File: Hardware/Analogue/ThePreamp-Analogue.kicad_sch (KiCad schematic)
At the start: 37 parts, among them IC1 ULN2803CDWR, J1 To preamp, J10 Switch & trigger outputs and 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, J11 Conn_01x04, J12 Conn_01x03, J13 Conn_01x04, J14 Conn_01x03, J15 Conn_01x02_Pin, J2 From preamp, J3 Digital In, J4 Digital Pass Through, J5 Conn_01x03_Pin, J9 ADS1115, K1 Input 1, K2 Input 5 (opt.), K3 Input 2, K4 Input 3, K5 Input 4, K6 Output Mute, K7 Trigger 1, K8 Trigger 2, U1 MCP23008-E_SO

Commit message: Chassis placement new draft
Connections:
- net +12V: now also J3.12 (Pin_12), J3.14 (Pin_14), J3.16 (Pin_16); no longer J3.2 (Pin_2), J3.4 (Pin_4)
- net +3.3V: now also J3.8 (Pin_8)
- net GND: now also J3.2 (Pin_2), J3.4 (Pin_4); no longer J3.12 (Pin_12), J3.14 (Pin_14), J3.16 (Pin_16), J3.8 (Pin_8)
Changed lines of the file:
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@@
 	)
 	(junction
-		(at 128.27 238.252)
-		(diameter 0)
-		(color 0 0 0 0)
-	)
-	(junction
-		(at 125.73 220.472)
-		(diameter 0)
-		(color 0 0 0 0)
-	)
-	(junction
 		(at 327.66 63.5)
 		(diameter 0)
@@
 	)
 	(junction
-		(at 131.318 225.552)
+		(at 128.27 221.742)
 		(diameter 0)
 		(color 0 0 0 0)
 	)
 	(junction
-		(at 128.27 235.712)
+		(at 128.27 228.092)
 		(diameter 0)
 		(color 0 0 0 0)
 	)
 	(junction
-		(at 128.27 233.172)
+		(at 128.27 235.712)
 		(diameter 0)
 		(color 0 0 0 0)
@@
 	(wire
 		(pts
-			(xy 131.318 230.632) (xy 131.318 225.552)
+			(xy 128.27 230.632) (xy 128.27 228.092)
 		)
 		(stroke
@@
 	(wire
 		(pts
-			(xy 335.28 67.31) (xy 354.33 67.31)
+			(xy 128.27 220.472) (xy 125.73 220.472)
 		)
 		(stroke
@@
 	(wire
 		(pts
-			(xy 86.614 200.66) (xy 99.06 200.66)
+			(xy 335.28 67.31) (xy 354.33 67.31)
 		)
 		(stroke
@@
 	(wire
 		(pts
-			(xy 262.382 71.12) (xy 262.382 73.66)
+			(xy 86.614 200.66) (xy 99.06 200.66)
 		)
 		(stroke
@@
 	(wire
 		(pts
-			(xy 131.064 238.252) (xy 128.27 238.252)
+			(xy 262.382 71.12) (xy 262.382 73.66)
 		)
 		(stroke
@@
 	(wire
 		(pts
-			(xy 128.27 228.092) (xy 128.27 233.172)
-		)
-		(stroke
-			(width 0)
-			(type default)
-		)
-	)
-	(wire
-		(pts
 			(xy 125.73 233.172) (xy 128.27 233.172)
 		)
@@
 	(wire
 		(pts
-			(xy 125.73 230.632) (xy 131.318 230.632)
+			(xy 125.73 230.632) (xy 128.27 230.632)
 		)
 		(stroke
@@
 	(wire
 		(pts
-			(xy 125.73 223.012) (xy 125.73 220.472)
+			(xy 128.27 228.092) (xy 128.27 225.552)
+		)
+		(stroke
+			(width 0)
+			(type default)
+		)
+	)
+	(wire
+		(pts
+			(xy 128.27 223.012) (xy 128.27 221.742)
 		)
 		(stroke
@@
 	(wire
 		(pts
+			(xy 128.27 223.012) (xy 125.73 223.012)
+		)
+		(stroke
+			(width 0)
+			(type default)
+		)
+	)
+	(wire
+		(pts
 			(xy 327.66 59.69) (xy 327.66 63.5)
 		)
@@
 	(wire
 		(pts
-			(xy 125.73 225.552) (xy 131.318 225.552)
+			(xy 125.73 225.552) (xy 128.27 225.552)
 		)
 		(stroke
@@
 	(wire
 		(pts
-			(xy 125.73 220.472) (xy 125.73 220.218)
+			(xy 128.27 221.742) (xy 128.27 220.472)
 		)
 		(stroke
@@
 		)
 	)
-	(wire
-		(pts
-			(xy 125.73 220.218) (xy 131.318 220.218)
-		)
-		(stroke
-			(width 0)
-			(type default)
-		)
-	)
 	(text "https://ez.analog.com/interface-isolation/f/q-a/568260/spi-bus-with-adum1401"
 		(exclude_from_sim no)
@@
 		(lib_name "+12V_1")
 		(lib_id "power:+12V")
-		(at 131.318 220.218 270)
+		(at 128.27 235.712 270)
 		(unit 1)
 		(exclude_from_sim no)
@@
 		(fields_autoplaced yes)
 		(property "Reference" "#PWR023"
-			(at 127.508 220.218 0)
+			(at 124.46 235.712 0)
 			(effects
 				(font
@@
 		)
 		(property "Value" "+12V"
-			(at 134.493 220.218 90)
+			(at 131.445 235.712 90)
 			(effects
 				(font
@@
 		)
 		(property "Footprint" ""
-			(at 131.318 220.218 0)
+			(at 128.27 235.712 0)
 			(effects
 				(font
@@
 		)
 		(property "Datasheet" ""
-			(at 131.318 220.218 0)
+			(at 128.27 235.712 0)
 			(effects
 				(font
@@
 		)
 		(property "Description" "Power symbol creates a global label with name \"+12V\""
-			(at 131.318 220.218 0)
+			(at 128.27 235.712 0)
 			(effects
 				(font
@@
 	(symbol
 		(lib_id "power:+3.3V")
-		(at 131.318 225.552 270)
+		(at 128.27 228.092 270)
 		(unit 1)
 		(exclude_from_sim no)
@@
 		(fields_autoplaced yes)
 		(property "Reference" "#PWR022"
-			(at 127.508 225.552 0)
+			(at 124.46 228.092 0)
 			(effects
 				(font
@@
 		)
 		(property "Value" "+3.3V"
-			(at 134.493 225.552 90)
+			(at 131.445 228.092 90)
 			(effects
 				(font
@@
 		)
 		(property "Footprint" ""
-			(at 131.318 225.552 0)
+			(at 128.27 228.092 0)
 			(effects
 				(font
@@
 		)
 		(property "Datasheet" ""
-			(at 131.318 225.552 0)
+			(at 128.27 228.092 0)
 			(effects
 				(font
@@
 		)
 		(property "Description" ""
-			(at 131.318 225.552 0)
+			(at 128.27 228.092 0)
 			(effects
 				(font
@@
 	(symbol
 		(lib_id "power:GND")
-		(at 131.064 238.252 90)
+		(at 128.27 221.742 90)
 		(unit 1)
 		(exclude_from_sim no)
@@
 		(dnp no)
 		(property "Reference" "#PWR021"
-			(at 137.414 238.252 0)
+			(at 134.62 221.742 0)
 			(effects
 				(font
@@
 		)
 		(property "Value" "GND"
-			(at 134.3152 238.125 90)
+			(at 131.5212 221.615 90)
 			(effects
 				(font
@@
 		)
 		(property "Footprint" ""
-			(at 131.064 238.252 0)
+			(at 128.27 221.742 0)
 			(effects
 				(font
@@
 		)
 		(property "Datasheet" ""
-			(at 131.064 238.252 0)
+			(at 128.27 221.742 0)
 			(effects
 				(font
@@
 		)
 		(property "Description" ""
-			(at 131.064 238.252 0)
+			(at 128.27 221.742 0)
 			(effects
 				(font

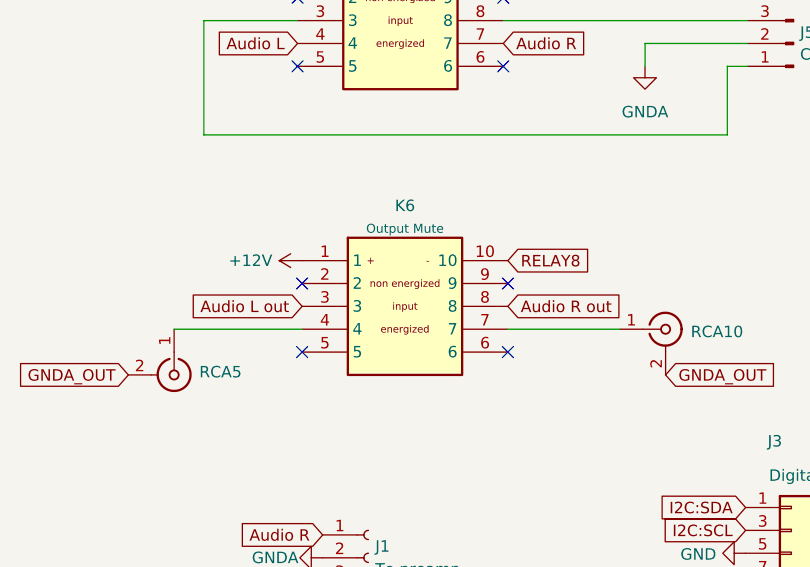
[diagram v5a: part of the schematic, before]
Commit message: pcb bug output relay fixed - when off output should be shorted to ground a
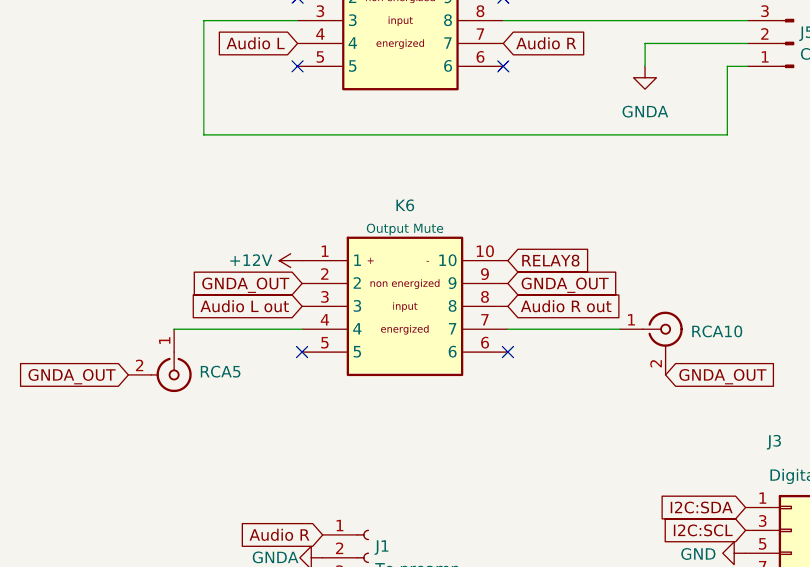
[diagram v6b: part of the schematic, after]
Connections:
- net GNDA_OUT: now also K6.2, K6.9
- no-connect marks 38 -> 36
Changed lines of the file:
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@@
-	)
-	(no_connect
-		(at 86.614 195.58)
 	)
 	(no_connect
@@
 	(no_connect
 		(at 359.156 178.562)
-	)
-	(no_connect
-		(at 63.754 195.58)
 	)
 	(no_connect
@@
 		)
 	)
+	(global_label "GNDA_OUT"
+		(shape input)
+		(at 63.754 195.58 180)
+		(fields_autoplaced yes)
+		(effects
+			(font
+				(size 1.27 1.27)
+			)
+			(justify right)
+		)
+		(property "Intersheetrefs" "${INTERSHEET_REFS}"
+			(at 51.8677 195.58 0)
+			(effects
+				(font
+					(size 1.27 1.27)
+				)
+				(justify right)
+				(hide yes)
+			)
+		)
+	)
 	(global_label "RELAY7"
 		(shape input)
@@
 			(effects
 				(font
+					(size 1.27 1.27)
+				)
+				(justify left)
+				(hide yes)
+			)
+		)
+	)
+	(global_label "GNDA_OUT"
+		(shape input)
+		(at 86.614 195.58 0)
+		(fields_autoplaced yes)
+		(effects
+			(font
+				(size 1.27 1.27)
+			)
+			(justify left)
+		)
+		(property "Intersheetrefs" "${INTERSHEET_REFS}"
+			(at 98.5003 195.58 0)
+			(effects
+				(font

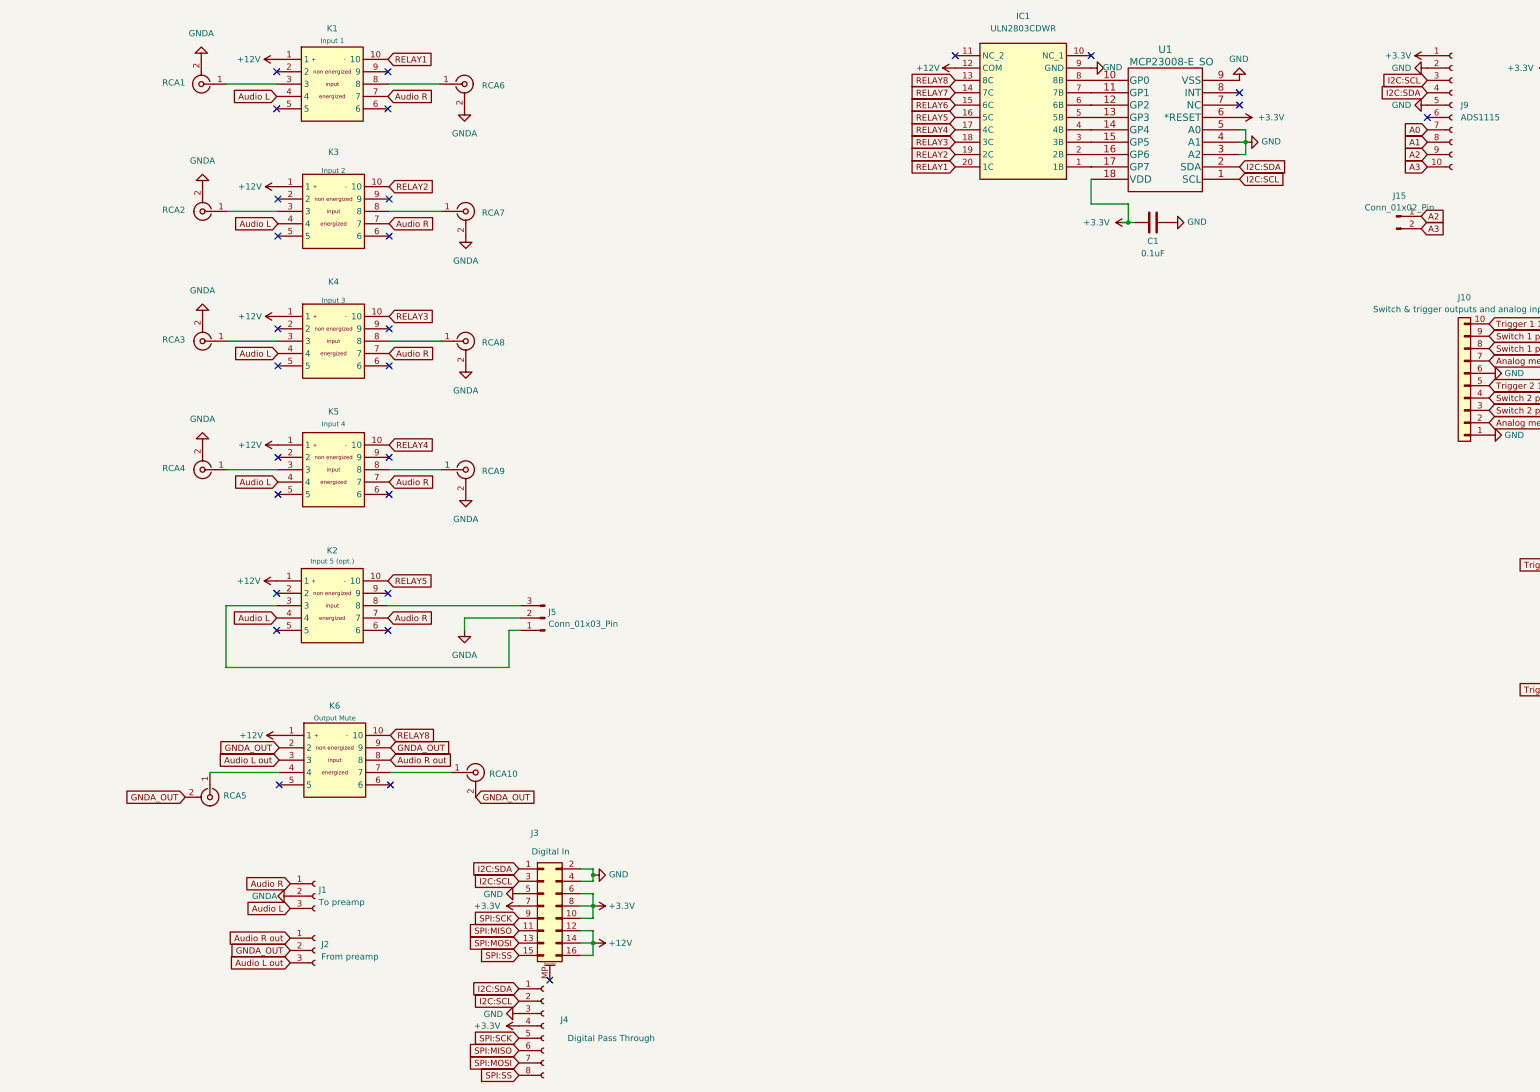
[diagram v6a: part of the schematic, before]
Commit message: Fixed output relay wiring on analog board schematic & pcb
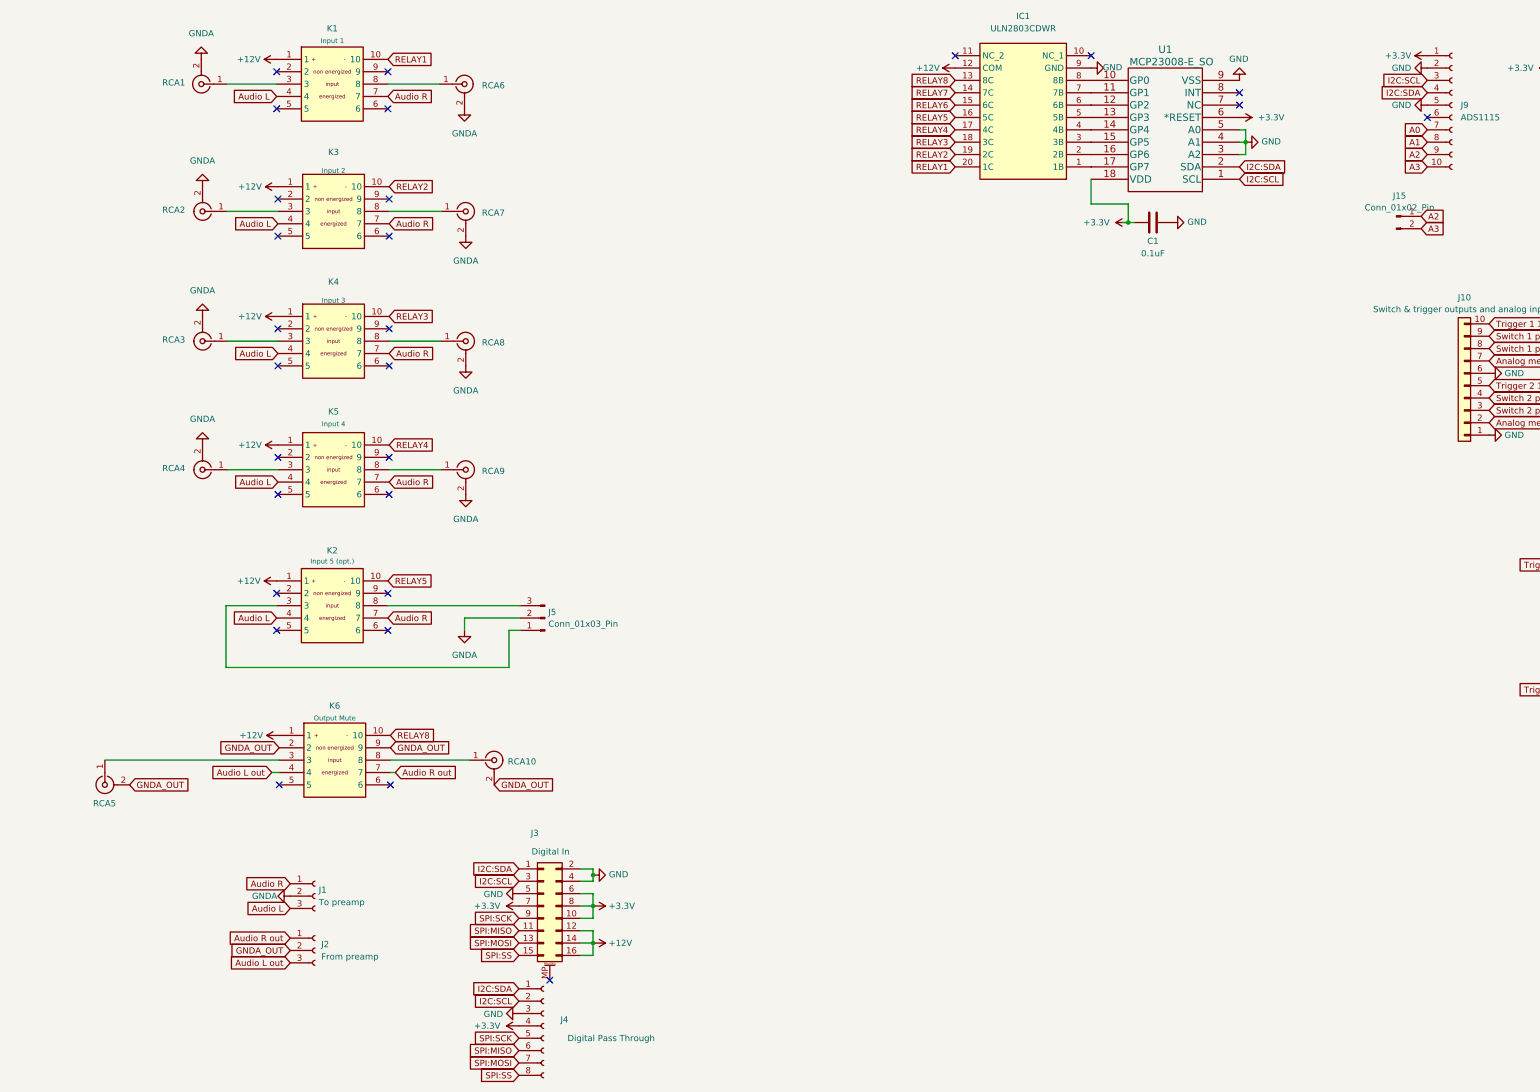
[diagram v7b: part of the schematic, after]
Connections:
- net Audio L out: now also K6.4; no longer K6.3
- net Audio R out: now also K6.7; no longer K6.8
- net at RCA10.1 (In): now also K6.8; no longer K6.7
- net at RCA5.1 (In): now also K6.3; no longer K6.4
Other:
- moved on the sheet: RCA10, RCA5
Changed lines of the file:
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@@
 (kicad_sch
-	(version 20231120)
+	(version 20250114)
 	(generator "eeschema")
-	(generator_version "8.0")
+	(generator_version "9.0")
 	(paper "A3")
+	(text "https://ez.analog.com/interface-isolation/f/q-a/568260/spi-bus-with-adum1401"
+		(exclude_from_sim no)
+		(at -86.106 87.376 0)
+		(effects
+			(font
+				(size 1.27 1.27)
+			)
+			(justify left bottom)
+		)
+	)
 	(junction
 		(at 238.252 87.63)
@@
 	(wire
 		(pts
-			(xy 86.614 200.66) (xy 99.06 200.66)
-		)
-		(stroke
-			(width 0)
-			(type default)
-		)
-	)
-	(wire
-		(pts
 			(xy 262.382 71.12) (xy 262.382 73.66)
 		)
@@
 	(wire
 		(pts
+			(xy 27.94 198.12) (xy 63.754 198.12)
+		)
+		(stroke
+			(width 0)
+			(type default)
+		)
+	)
+	(wire
+		(pts
 			(xy 349.25 63.5) (xy 349.25 71.12)
 		)
@@
 	(wire
 		(pts
+			(xy 86.614 200.66) (xy 87.63 200.66)
+		)
+		(stroke
+			(width 0)
+			(type default)
+		)
+	)
+	(wire
+		(pts
 			(xy 125.73 230.632) (xy 128.27 230.632)
 		)
@@
 	(wire
 		(pts
-			(xy 49.53 200.66) (xy 63.754 200.66)
+			(xy 52.832 166.37) (xy 52.832 179.07)
 		)
 		(stroke
@@
 	(wire
 		(pts
-			(xy 52.832 166.37) (xy 52.832 179.07)
+			(xy 52.832 179.07) (xy 110.998 179.07)
 		)
 		(stroke
@@
 	(wire
 		(pts
-			(xy 52.832 179.07) (xy 110.998 179.07)
+			(xy 52.832 59.182) (xy 63.246 59.182)
 		)
 		(stroke
@@
 	(wire
 		(pts
-			(xy 52.832 59.182) (xy 63.246 59.182)
+			(xy 128.27 235.712) (xy 128.27 238.252)
 		)
 		(stroke
@@
 	(wire
 		(pts
-			(xy 128.27 235.712) (xy 128.27 238.252)
+			(xy 86.614 198.12) (xy 102.87 198.12)
 		)
 		(stroke
@@
 	(wire
 		(pts
-			(xy 238.252 83.82) (xy 238.252 87.63)
+			(xy 62.23 200.66) (xy 63.754 200.66)
 		)
 		(stroke
@@
 		)
 	)
-	(text "https://ez.analog.com/interface-isolation/f/q-a/568260/spi-bus-with-adum1401"
-		(exclude_from_sim no)
-		(at -86.106 87.376 0)
-		(effects
-			(font
-				(size 1.27 1.27)
-			)
-			(justify left bottom)
+	(wire
+		(pts
+			(xy 238.252 83.82) (xy 238.252 87.63)
+		)
+		(stroke
+			(width 0)
+			(type default)
 		)
 	)
@@
 	(global_label "Audio L out"
 		(shape input)
-		(at 63.754 198.12 180)
+		(at 62.23 200.66 180)
 		(fields_autoplaced yes)
 		(effects
@@
 		)
 		(property "Intersheetrefs" "${INTERSHEET_REFS}"
-			(at 50.3022 198.0406 0)
+			(at 48.7782 200.5806 0)
 			(effects
 				(font
@@
 	(global_label "GNDA_OUT"
 		(shape input)
-		(at 44.45 205.74 180)
+		(at 33.02 203.2 0)
 		(fields_autoplaced yes)
 		(effects
@@
 				(size 1.27 1.27)
 			)
-			(justify right)
+			(justify left)
 		)
 		(property "Intersheetrefs" "${INTERSHEET_REFS}"
-			(at 32.5637 205.74 0)
+			(at 44.9063 203.2 0)
 			(effects
 				(font
 					(size 1.27 1.27)
 				)
-				(justify right)
+				(justify left)
 				(hide yes)
 			)
@@
 	(global_label "Audio R out"
 		(shape input)
-		(at 86.614 198.12 0)
+		(at 87.63 200.66 0)
 		(fields_autoplaced yes)
 		(effects
@@
 		)
 		(property "Intersheetrefs" "${INTERSHEET_REFS}"
-			(at 100.3077 198.0406 0)
+			(at 101.3237 200.5806 0)
 			(effects
 				(font
@@
 	(global_label "GNDA_OUT"
 		(shape input)
-		(at 104.14 205.74 0)
+		(at 107.95 203.2 0)
 		(fields_autoplaced yes)
 		(effects
@@
 		)
 		(property "Intersheetrefs" "${INTERSHEET_REFS}"
-			(at 116.0263 205.74 0)
+			(at 119.8363 203.2 0)
 			(effects
 				(font
@@
 	(symbol
 		(lib_id "RCA ALI:RCA_Connector_ALI")
-		(at 104.14 200.66 0)
+		(at 107.95 198.12 0)
 		(unit 1)
 		(exclude_from_sim no)
@@
 		(fields_autoplaced yes)
 		(property "Reference" "RCA10"
-			(at 106.934 200.9532 0)
+			(at 110.744 198.4132 0)
 			(effects
 				(font
@@
 		)
 		(property "Value" "RCA_Connector_ALI"
-			(at 107.061 200.66 90)
+			(at 110.871 198.12 90)
 			(effects
 				(font
@@
 		)
 		(property "Footprint" "RCA ALI:RCA Connector ALI"
-			(at 104.14 190.5 0)
+			(at 107.95 187.96 0)
 			(effects
 				(font
@@
 		)
 		(property "Datasheet" " ~"
-			(at 104.14 200.66 0)
+			(at 107.95 198.12 0)
 			(effects
 				(font
@@
 		)
 		(property "Description" ""
-			(at 104.14 200.66 0)
+			(at 107.95 198.12 0)
 			(effects
 				(font
@@
 	(symbol
 		(lib_id "RCA ALI:RCA_Connector_ALI")
-		(at 49.53 205.74 270)
+		(at 27.94 203.2 90)
+		(mirror x)
 		(unit 1)
 		(exclude_from_sim no)
@@
 		(on_board yes)
 		(dnp no)
-		(fields_autoplaced yes)
 		(property "Reference" "RCA5"
-			(at 52.324 205.4225 90)
+			(at 30.226 207.01 90)
 			(effects
 				(font
@@
 		)
 		(property "Value" "RCA_Connector_ALI"
-			(at 49.53 208.661 90)
+			(at 27.94 206.121 90)
 			(effects
 				(font
@@
 		)
 		(property "Footprint" "RCA ALI:RCA Connector ALI"
-			(at 59.69 205.74 0)
+			(at 17.78 203.2 0)
 			(effects
 				(font
@@
 		)
 		(property "Datasheet" " ~"
-			(at 49.53 205.74 0)
+			(at 27.94 203.2 0)
 			(effects
 				(font
@@
 		)
 		(property "Description" ""
-			(at 49.53 205.74 0)
+			(at 27.94 203.2 0)
 			(effects
 				(font
@@
 		)
 	)
+	(embedded_fonts no)
 )
